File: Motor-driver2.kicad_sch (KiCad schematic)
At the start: 47 parts, among them J12 PINHD_1x4_Male, J15 PINHD_1x4_Male, U4 DRV8825PWP, U5 DRV8825PWP

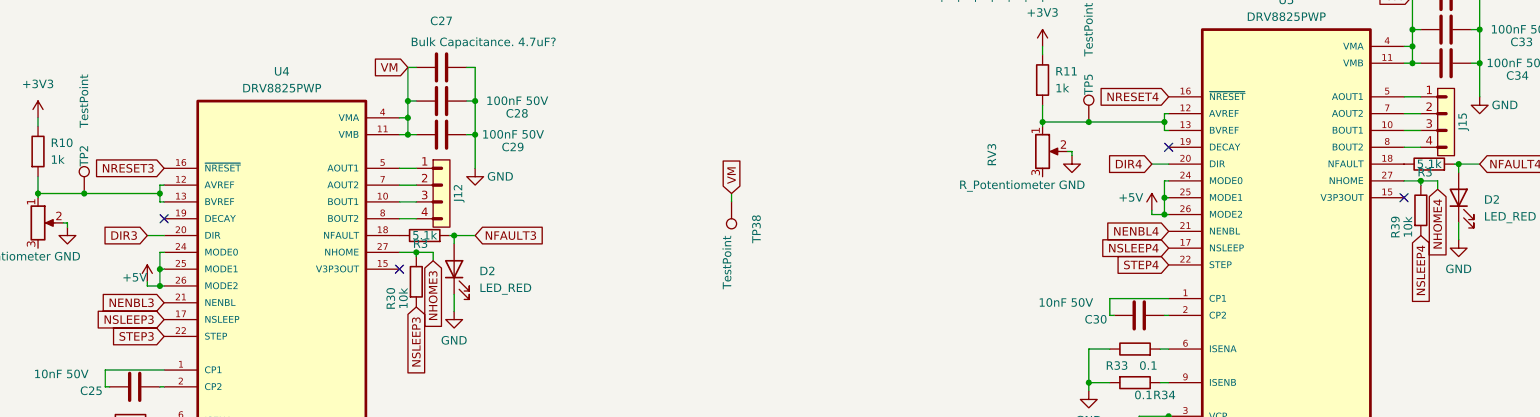
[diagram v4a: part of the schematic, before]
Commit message: routed some paths on schematic. need to rearrange driver pins and come up with solution with motor poer supply
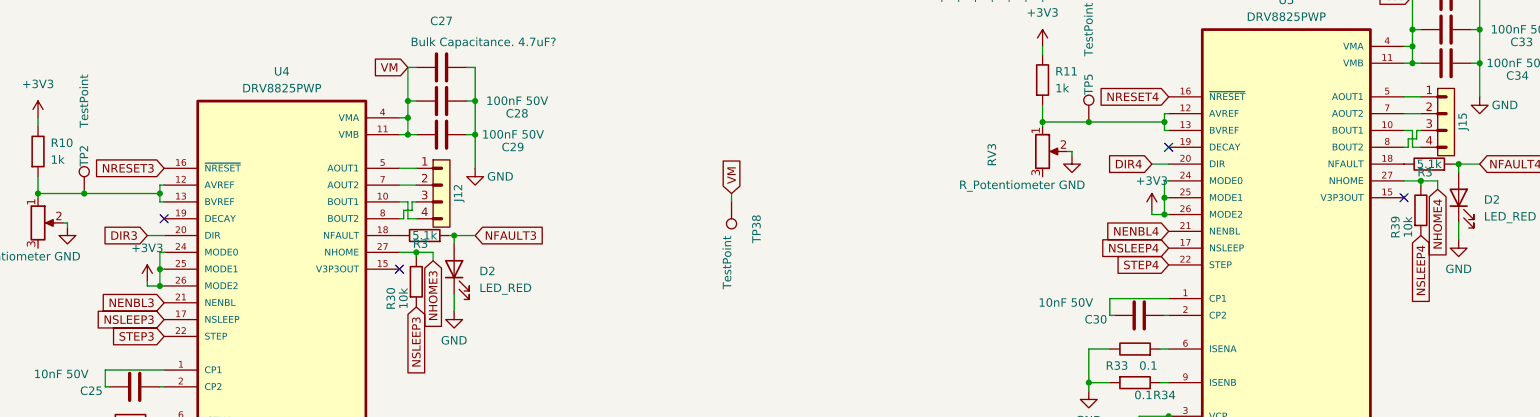
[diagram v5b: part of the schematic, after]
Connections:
- net +5V is gone; now on net +3V3: U4.24 (MODE0), U4.25 (MODE1), U4.26 (MODE2), U5.24 (MODE0), U5.25 (MODE1), U5.26 (MODE2)
- net at J15.3: now also U5.8 (BOUT2); no longer U5.10 (BOUT1)
- net at J15.4: now also U5.10 (BOUT1); no longer U5.8 (BOUT2)
- net at U4.10 (BOUT1): now also J12.4; no longer J12.3
- net at U4.8 (BOUT2): now also J12.3; no longer J12.4
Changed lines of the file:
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@@
+    (stroke (width 0) (type default))
+  )
+  (wire (pts (xy 88.265 106.045) (xy 88.265 104.775))
+    (stroke (width 0) (type default))
+  )
+  (wire (pts (xy 240.665 92.71) (xy 240.665 95.25))
     (stroke (width 0) (type default))
   )
@@
     (stroke (width 0) (type default))
   )
+  (wire (pts (xy 240.665 95.25) (xy 241.935 95.25))
+    (stroke (width 0) (type default))
+  )
   (wire (pts (xy 180.975 31.75) (xy 182.88 31.75))
     (stroke (width 0) (type default))
@@
     (stroke (width 0) (type default))
   )
+  (wire (pts (xy 239.395 92.71) (xy 240.665 92.71))
+    (stroke (width 0) (type default))
+  )
   (wire (pts (xy 184.785 88.9) (xy 184.785 91.44))
     (stroke (width 0) (type default))
@@
     (stroke (width 0) (type default))
   )
+  (wire (pts (xy 240.03 93.98) (xy 241.3 93.98))
+    (stroke (width 0) (type default))
+  )
   (wire (pts (xy 191.77 130.81) (xy 194.945 130.81))
     (stroke (width 0) (type default))
   )
-  (wire (pts (xy 241.935 92.71) (xy 239.395 92.71))
-    (stroke (width 0) (type default))
-  )
   (wire (pts (xy 52.07 100.965) (xy 51.435 100.965))
     (stroke (width 0) (type default))
@@
     (stroke (width 0) (type default))
   )
+  (wire (pts (xy 241.3 93.98) (xy 241.3 92.71))
+    (stroke (width 0) (type default))
+  )
   (wire (pts (xy 51.435 103.505) (xy 52.07 103.505))
     (stroke (width 0) (type default))
@@
     (stroke (width 0) (type default))
   )
-  (wire (pts (xy 90.17 106.045) (xy 87.63 106.045))
-    (stroke (width 0) (type default))
-  )
   (wire (pts (xy 239.395 82.55) (xy 240.665 82.55))
     (stroke (width 0) (type default))
@@
     (stroke (width 0) (type default))
   )
+  (wire (pts (xy 89.535 104.775) (xy 89.535 103.505))
+    (stroke (width 0) (type default))
+  )
   (wire (pts (xy 90.17 98.425) (xy 87.63 98.425))
     (stroke (width 0) (type default))
@@
     (stroke (width 0) (type default))
   )
+  (wire (pts (xy 88.9 106.045) (xy 90.17 106.045))
+    (stroke (width 0) (type default))
+  )
   (wire (pts (xy 250.825 77.47) (xy 250.825 82.55))
     (stroke (width 0) (type default))
@@
     (stroke (width 0) (type default))
   )
-  (wire (pts (xy 90.17 103.505) (xy 87.63 103.505))
-    (stroke (width 0) (type default))
-  )
   (wire (pts (xy 40.005 141.605) (xy 43.18 141.605))
     (stroke (width 0) (type default))
@@
     (stroke (width 0) (type default))
   )
+  (wire (pts (xy 239.395 95.25) (xy 240.03 95.25))
+    (stroke (width 0) (type default))
+  )
   (wire (pts (xy 88.9 83.185) (xy 88.9 88.265))
     (stroke (width 0) (type default))
@@
     (stroke (width 0) (type default))
   )
+  (wire (pts (xy 87.63 106.045) (xy 88.265 106.045))
+    (stroke (width 0) (type default))
+  )
   (wire (pts (xy 249.555 77.47) (xy 250.825 77.47))
     (stroke (width 0) (type default))
@@
     (stroke (width 0) (type default))
   )
+  (wire (pts (xy 241.3 92.71) (xy 241.935 92.71))
+    (stroke (width 0) (type default))
+  )
   (wire (pts (xy 201.295 97.79) (xy 203.835 97.79))
     (stroke (width 0) (type default))
@@
     (stroke (width 0) (type default))
   )
+  (wire (pts (xy 240.03 95.25) (xy 240.03 93.98))
+    (stroke (width 0) (type default))
+  )
   (wire (pts (xy 116.84 154.305) (xy 118.745 154.305))
     (stroke (width 0) (type default))
   )
+  (wire (pts (xy 88.9 103.505) (xy 88.9 106.045))
+    (stroke (width 0) (type default))
+  )
+  (wire (pts (xy 88.265 104.775) (xy 89.535 104.775))
+    (stroke (width 0) (type default))
+  )
   (wire (pts (xy 40.005 102.235) (xy 51.435 102.235))
     (stroke (width 0) (type default))
@@
     (stroke (width 0) (type default))
   )
+  (wire (pts (xy 89.535 103.505) (xy 90.17 103.505))
+    (stroke (width 0) (type default))
+  )
   (wire (pts (xy 33.02 99.695) (xy 33.02 102.235))
     (stroke (width 0) (type default))
@@
     (stroke (width 0) (type default))
   )
-  (wire (pts (xy 241.935 95.25) (xy 239.395 95.25))
-    (stroke (width 0) (type default))
-  )
   (wire (pts (xy 180.975 26.67) (xy 182.88 26.67))
     (stroke (width 0) (type default))
   )
   (wire (pts (xy 116.84 151.765) (xy 118.745 151.765))
+    (stroke (width 0) (type default))
+  )
+  (wire (pts (xy 87.63 103.505) (xy 88.9 103.505))
     (stroke (width 0) (type default))
   )
@@
     )
   )
+  (symbol (lib_id "power:+3V3") (at 201.295 104.775 0) (unit 1)
+    (in_bom yes) (on_board yes) (dnp no) (fields_autoplaced)
+    (property "Reference" "#PWR049" (at 201.295 108.585 0)
+      (effects (font (size 1.27 1.27)) hide)
+    )
+    (property "Value" "+3V3" (at 201.295 100.33 0)
+      (effects (font (size 1.27 1.27)))
+    )
+    (property "Footprint" "" (at 201.295 104.775 0)
+      (effects (font (size 1.27 1.27)) hide)
+    )
+    (property "Datasheet" "" (at 201.295 104.775 0)
+      (effects (font (size 1.27 1.27)) hide)
+    )
+    (pin "1")
+    (instances
+      (project "Doodle Drive"
+        (path "/3ec634aa-8c09-482d-9325-2288a4dbd68b/4a4951fa-be57-4d48-97a5-6be750b353b5"
+          (reference "#PWR049") (unit 1)
+        )
+      )
+    )
+  )
   (symbol (lib_id "Device:C") (at 52.07 153.035 180) (unit 1)
     (in_bom yes) (on_board yes) (dnp no)
@@
         (path "/3ec634aa-8c09-482d-9325-2288a4dbd68b/4a4951fa-be57-4d48-97a5-6be750b353b5"
           (reference "TP35") (unit 1)
-        )
-      )
-    )
-  )
-  (symbol (lib_id "power:+5V") (at 49.53 115.57 0) (unit 1)
-    (in_bom yes) (on_board yes) (dnp no)
-    (property "Reference" "#PWR049" (at 49.53 119.38 0)
-      (effects (font (size 1.27 1.27)) hide)
-    )
-    (property "Value" "+5V" (at 47.625 114.935 0)
-      (effects (font (size 1.27 1.27)))
-    )
-    (property "Footprint" "" (at 49.53 115.57 0)
-      (effects (font (size 1.27 1.27)) hide)
-    )
-    (property "Datasheet" "" (at 49.53 115.57 0)
-      (effects (font (size 1.27 1.27)) hide)
-    )
-    (pin "1")
-    (instances
-      (project "Doodle Drive"
-        (path "/3ec634aa-8c09-482d-9325-2288a4dbd68b/4a4951fa-be57-4d48-97a5-6be750b353b5"
-          (reference "#PWR049") (unit 1)
         )
       )
@@
     )
   )
+  (symbol (lib_id "power:+3V3") (at 49.53 115.57 0) (unit 1)
+    (in_bom yes) (on_board yes) (dnp no) (fields_autoplaced)
+    (property "Reference" "#PWR056" (at 49.53 119.38 0)
+      (effects (font (size 1.27 1.27)) hide)
+    )
+    (property "Value" "+3V3" (at 49.53 110.49 0)
+      (effects (font (size 1.27 1.27)))
+    )
+    (property "Footprint" "" (at 49.53 115.57 0)
+      (effects (font (size 1.27 1.27)) hide)
+    )
+    (property "Datasheet" "" (at 49.53 115.57 0)
+      (effects (font (size 1.27 1.27)) hide)
+    )
+    (pin "1")
+    (instances
+      (project "Doodle Drive"
+        (path "/3ec634aa-8c09-482d-9325-2288a4dbd68b/4a4951fa-be57-4d48-97a5-6be750b353b5"
+          (reference "#PWR056") (unit 1)
+        )
+      )
+    )
+  )
   (symbol (lib_id "Connector:TestPoint") (at 180.34 55.245 180) (unit 1)
     (in_bom yes) (on_board yes) (dnp no)
@@
         )
       )
-    )
-  )
-  (symbol (lib_id "power:+5V") (at 201.295 104.775 0) (unit 1)
-    (in_bom yes) (on_board yes) (dnp no)
-    (property "Reference" "#PWR056" (at 201.295 108.585 0)
-      (effects (font (size 1.27 1.27)) hide)
-    )
-    (property "Value" "+5V" (at 198.12 102.87 0)
-      (effects (font (size 1.27 1.27)))
-    )
-    (property "Footprint" "" (at 201.295 104.775 0)
-      (effects (font (size 1.27 1.27)) hide)
-    )
-    (property "Datasheet" "" (at 201.295 104.775 0)
-      (effects (font (size 1.27 1.27)) hide)
-    )
-    (pin "1")
-    (instances
-      (project "Doodle Drive"
-        (path "/3ec634aa-8c09-482d-9325-2288a4dbd68b/4a4951fa-be57-4d48-97a5-6be750b353b5"
-          (reference "#PWR056") (unit 1)
-        )
-      )

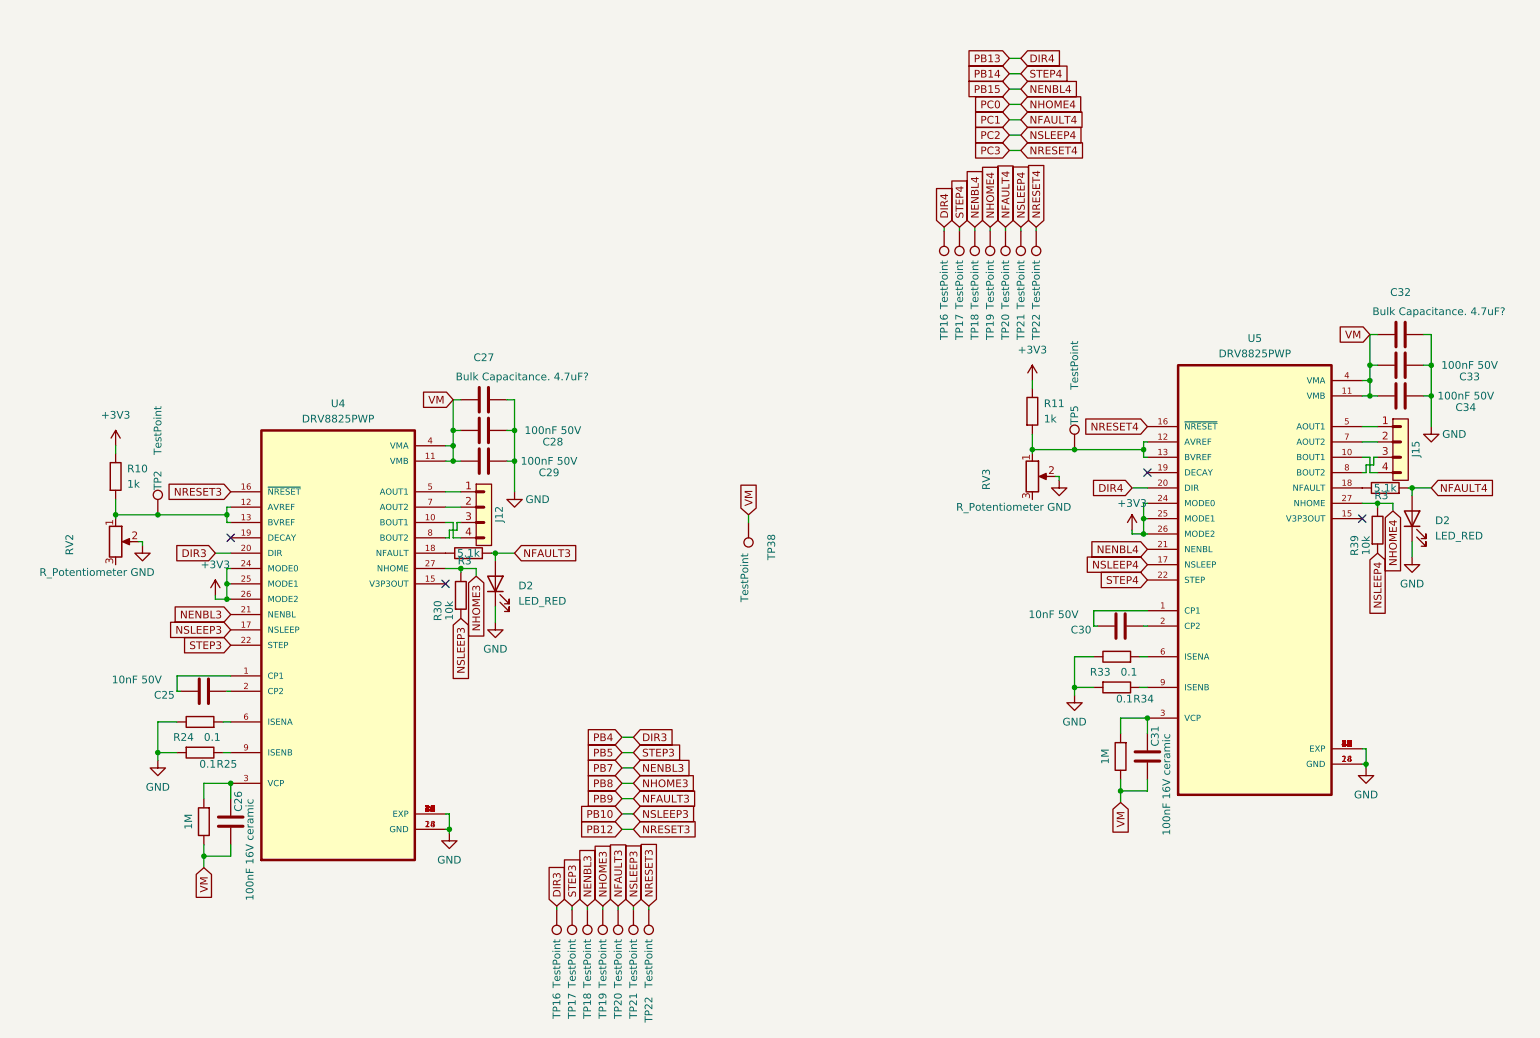
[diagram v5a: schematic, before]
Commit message: temporarly detached testpoints
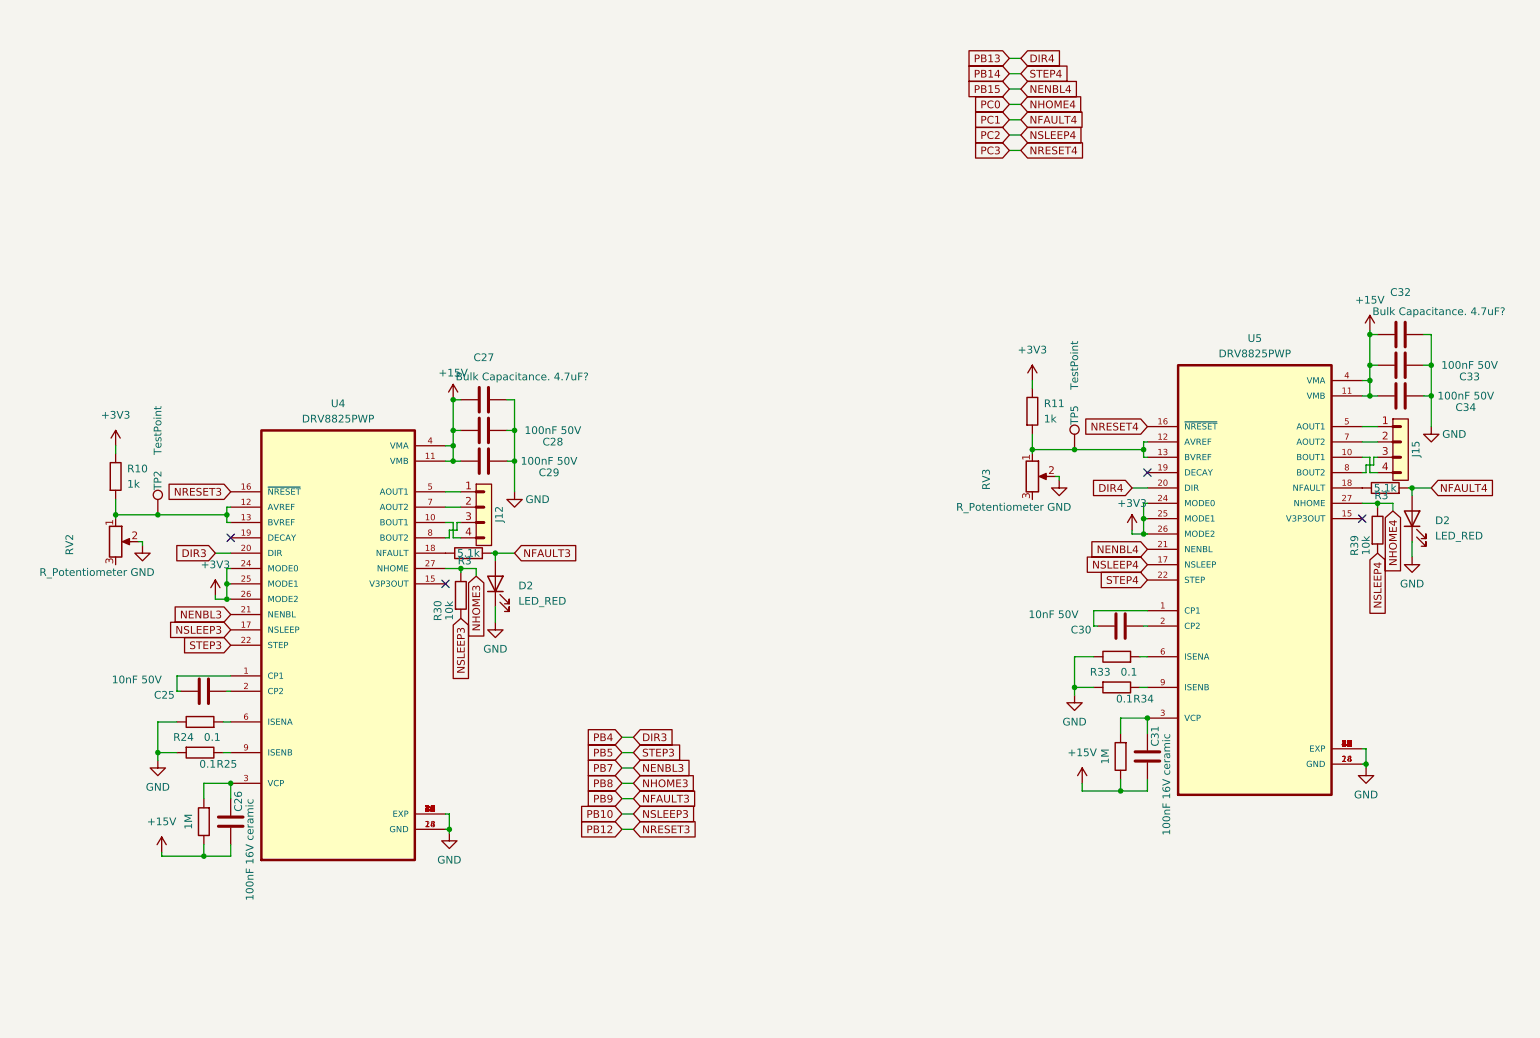
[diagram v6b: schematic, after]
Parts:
- removed TP16 (x2), TP17 (x2), TP18 (x2), TP19 (x2), TP20 (x2), TP21 (x2), TP22 (x2), TP38: TestPoint, TestPoint:TestPoint_Pad_D2.5mm, symbol Connector:TestPoint
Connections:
- net VM renamed +15V

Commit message: routet Motor Driver modules, reattached and placed testpoints
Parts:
- C26, C31: footprint Capacitor_SMD:C_01005_0402Metric -> Capacitor_SMD:C_0402_1005Metric
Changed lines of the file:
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@@
       (effects (font (size 1.27 1.27)) (justify left))
     )
-    (property "Footprint" "Capacitor_SMD:C_01005_0402Metric" (at 51.1048 149.225 0)
+    (property "Footprint" "Capacitor_SMD:C_0402_1005Metric" (at 51.1048 149.225 0)
       (effects (font (size 1.27 1.27)) hide)
     )
@@
       (effects (font (size 1.27 1.27)) (justify left))
     )
-    (property "Footprint" "Capacitor_SMD:C_01005_0402Metric" (at 202.8698 138.43 0)
-      (effects (font (size 1.27 1.27)) hide)
-    )
+    (property "Footprint" "Capacitor_SMD:C_0402_1005Metric" (at 202.8698 138.43 0)
+      (effects (font (size 1.27 1.27)) hide)
+    )
